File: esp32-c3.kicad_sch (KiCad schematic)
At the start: 11 parts, among them J7 Lichtenprog_conn, Q1 MMBT2222A, Q2 MMBT2222A, U3 ESP32-C3-WROOM-02

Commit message: save before charger replace
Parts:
- renumbered C5 to C15, C6 to C16, J7 to J4, Q1 to Q2, Q2 to Q3, R21 to R15, R25 to R16, R26 to R17, U3 to U7
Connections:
- net +3.3V is gone; now on net 3V3: R15.2

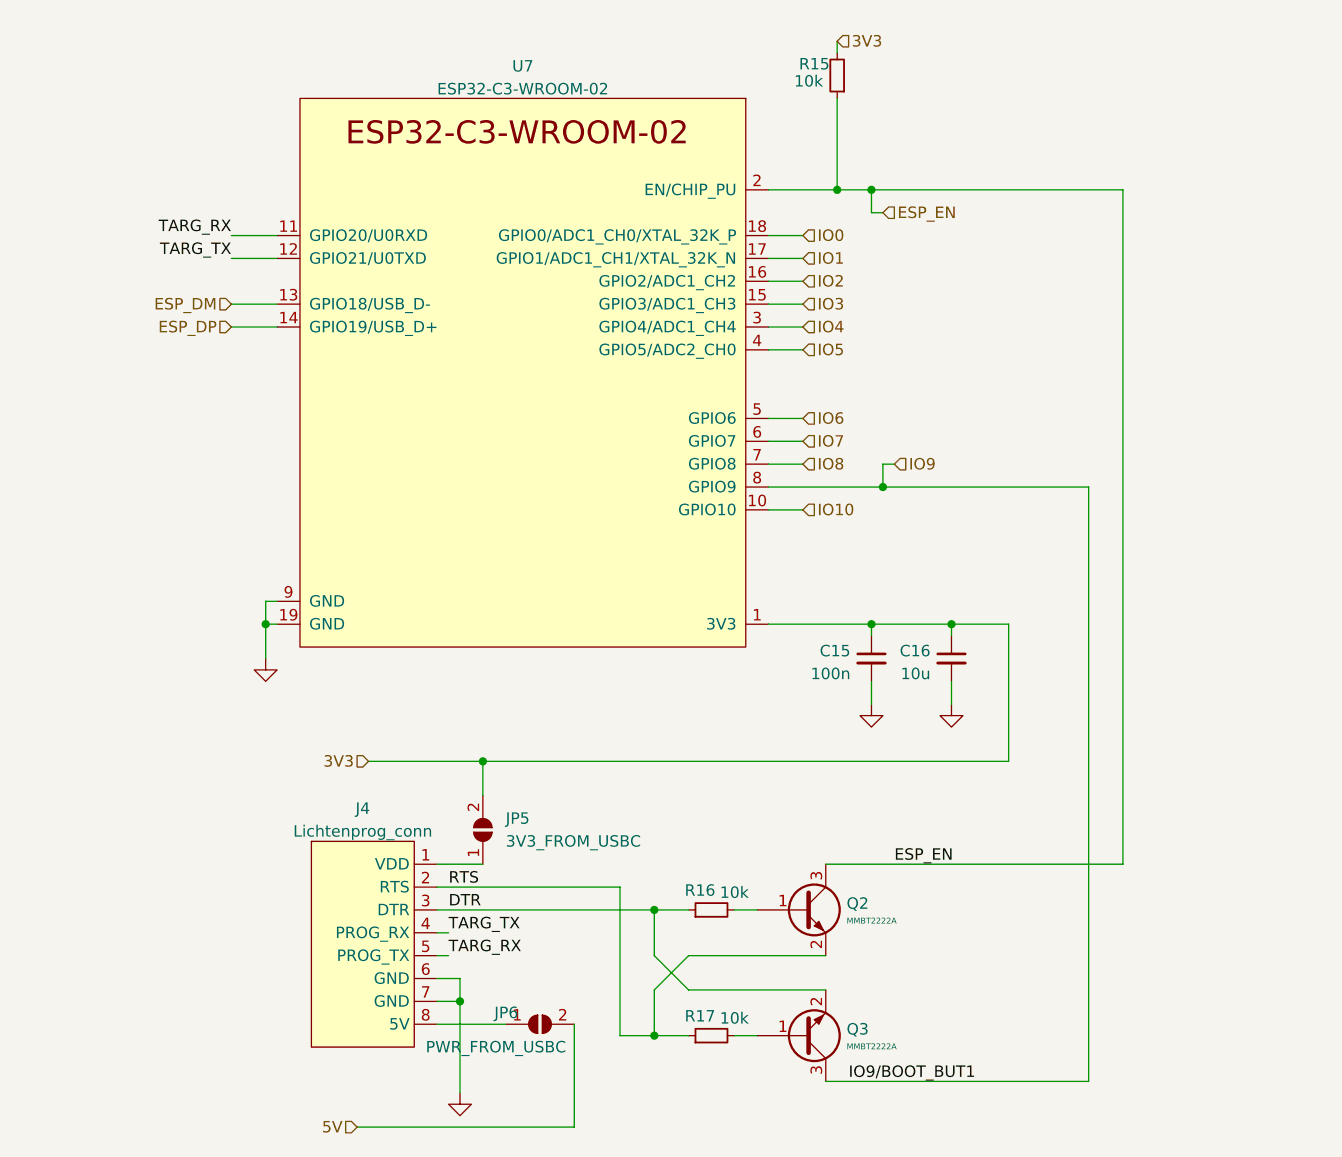
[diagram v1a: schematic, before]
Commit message: connector placement
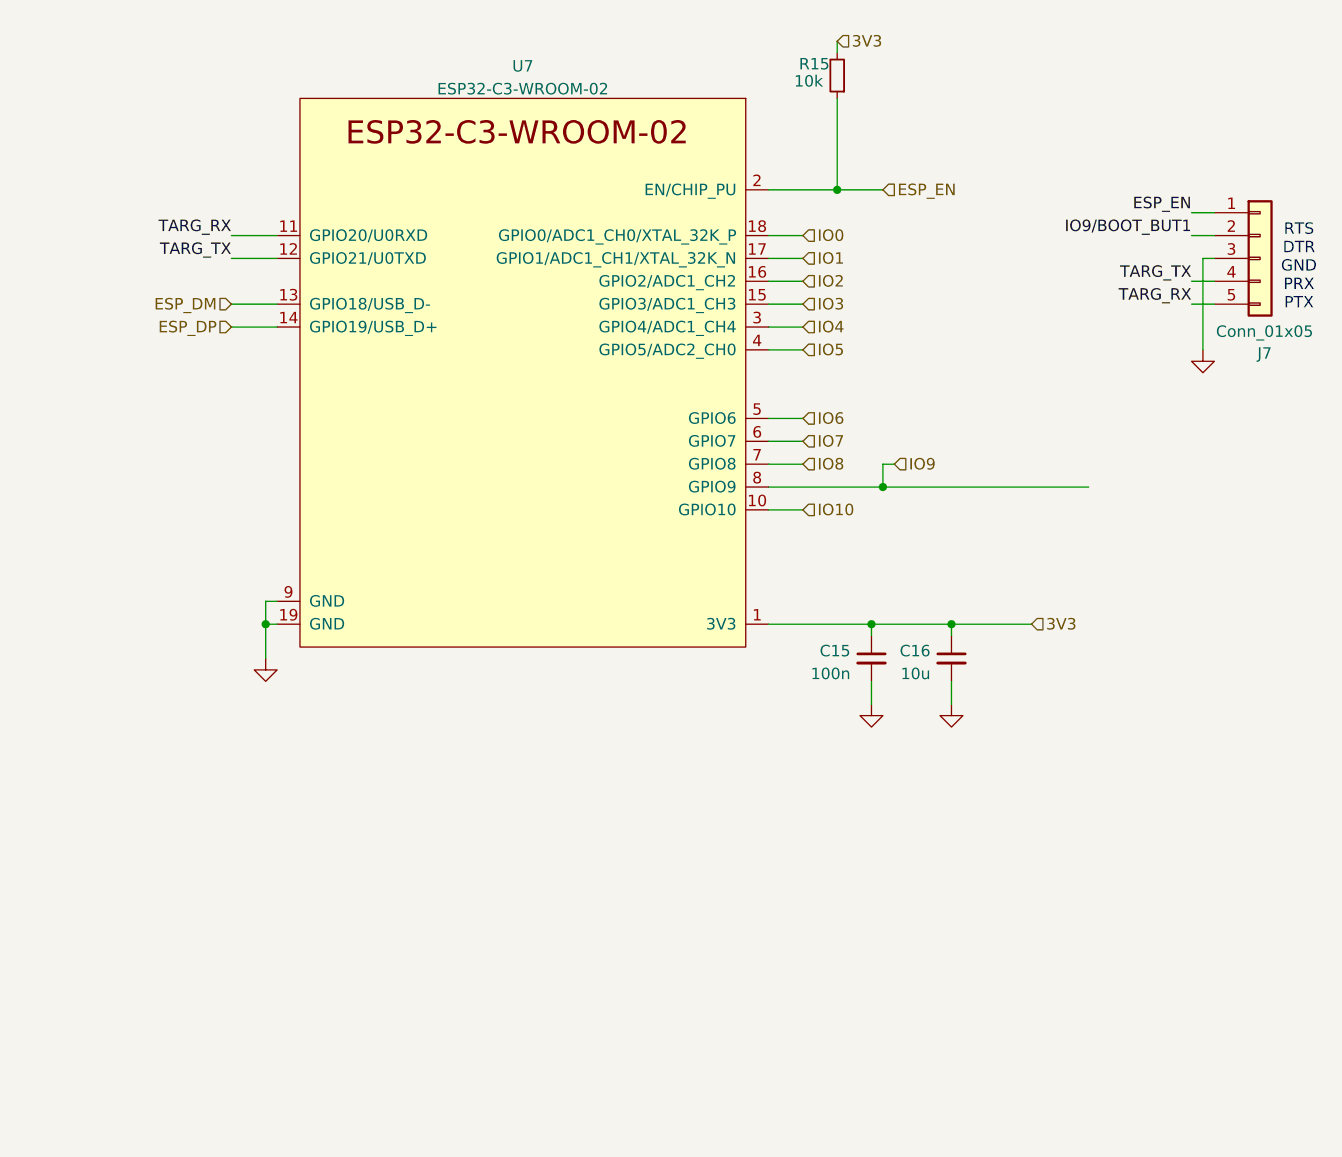
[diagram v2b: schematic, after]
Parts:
- removed J4: Lichtenprog_conn, Critbit_lib:Lichtenprog, symbol Critbit_lib:Lichtenprog_conn
- removed JP5: 3V3_FROM_USBC, Jumper:SolderJumper-2_P1.3mm_Open_TrianglePad1.0x1.5mm, symbol Jumper:SolderJumper_2_Open
- removed JP6: PWR_FROM_USBC, Jumper:SolderJumper-2_P1.3mm_Open_TrianglePad1.0x1.5mm, symbol Jumper:SolderJumper_2_Open
- removed Q2, Q3: MMBT2222A, Package_TO_SOT_SMD:SOT-23, symbol Device:Q_NPN_BEC
- removed R16, R17: 10k, Resistor_SMD:R_0402_1005Metric, symbol Device:R_Small
- added J7: Conn_01x05, Connector_PinHeader_1.27mm:PinHeader_1x05_P1.27mm_Vertical, symbol Connector_Generic:Conn_01x05
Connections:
- net ESP_EN: now also J7.1 (Pin_1)
- net GND: now also J7.3 (Pin_3)
- net TARG_RX: now also J7.5 (Pin_5)
- net TARG_TX: now also J7.4 (Pin_4)
- new net IO9/BOOT_BUT1: J7.2 (Pin_2)
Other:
- note added: "RTS DTR GND PRX PTX"

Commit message: adadadadadadadadadada
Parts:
- C15: LCSC C307331 -> (none)
- C16: LCSC C15525 -> (none)
- R15: LCSC C25744 -> (none)
- U7: LCSC DNP -> (none)
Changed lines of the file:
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@@
-			)
-		)
-		(property "LCSC" "DNP"
-			(at 68.58 96.52 0)
-			(effects
-				(font
-					(size 1.27 1.27)
-				)
-				(hide yes)
 			)
 		)
@@
 			)
 		)
-		(property "LCSC" "C15525"
-			(at 115.57 127 0)
-			(effects
-				(font
-					(size 1.27 1.27)
-				)
-				(hide yes)
-			)
-		)
 		(pin "1"
 		)
@@
 			)
 		)
-		(property "LCSC" "C25744"
-			(at 102.87 62.23 0)
-			(effects
-				(font
-					(size 1.27 1.27)
-				)
-				(hide yes)
-			)
-		)
 		(pin "1"
 		)
@@
 			(at 106.68 127 0)
 			(effects
-				(font
-					(size 1.27 1.27)
-				)
-				(hide yes)
-			)
-		)
-		(property "LCSC" "C307331"
-			(at 106.68 127 0)
-			(effects

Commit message: do backup kids
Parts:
- C16: footprint Capacitor_SMD:C_0402_1005Metric -> Capacitor_SMD:C_0603_1608Metric
- J7: footprint Connector_PinHeader_1.27mm:PinHeader_1x05_P1.27mm_Vertical -> Critbit_lib:sideclutch
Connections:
- net IO9/BOOT_BUT1 is gone; now on net IO9: J7.2 (Pin_2)
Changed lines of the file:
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@@
+	)
+	(junction
+		(at 105.41 74.93)
+		(diameter 0)
+		(color 0 0 0 0)
 	)
 	(junction
@@
 	(wire
 		(pts
+			(xy 130.81 107.95) (xy 130.81 80.01)
+		)
+		(stroke
+			(width 0)
+			(type default)
+		)
+	)
+	(wire
+		(pts
 			(xy 99.06 85.09) (xy 95.25 85.09)
 		)
@@
 	(wire
 		(pts
+			(xy 105.41 74.93) (xy 107.95 74.93)
+		)
+		(stroke
+			(width 0)
+			(type default)
+		)
+	)
+	(wire
+		(pts
 			(xy 109.22 105.41) (xy 107.95 105.41)
 		)
@@
 	(wire
 		(pts
+			(xy 130.81 80.01) (xy 144.78 80.01)
+		)
+		(stroke
+			(width 0)
+			(type default)
+		)
+	)
+	(wire
+		(pts
 			(xy 99.06 100.33) (xy 95.25 100.33)
 		)
@@
 	(wire
 		(pts
+			(xy 105.41 77.47) (xy 105.41 74.93)
+		)
+		(stroke
+			(width 0)
+			(type default)
+		)
+	)
+	(wire
+		(pts
 			(xy 99.06 87.63) (xy 95.25 87.63)
 		)
@@
 	(wire
 		(pts
-			(xy 142.24 80.01) (xy 144.78 80.01)
-		)
-		(stroke
-			(width 0)
-			(type default)
-		)
-	)
-	(wire
-		(pts
 			(xy 106.68 129.54) (xy 106.68 132.08)
 		)
@@
 	(wire
 		(pts
+			(xy 105.41 77.47) (xy 144.78 77.47)
+		)
+		(stroke
+			(width 0)
+			(type default)
+		)
+	)
+	(wire
+		(pts
 			(xy 107.95 105.41) (xy 107.95 107.95)
 		)
@@
 	(wire
 		(pts
-			(xy 142.24 77.47) (xy 144.78 77.47)
-		)
-		(stroke
-			(width 0)
-			(type default)
-		)
-	)
-	(wire
-		(pts
 			(xy 107.95 107.95) (xy 130.81 107.95)
 		)
@@
 	(wire
 		(pts
-			(xy 102.87 74.93) (xy 107.95 74.93)
+			(xy 102.87 74.93) (xy 105.41 74.93)
 		)
 		(stroke
@@
 				(size 1.27 1.27)
 			)
-		)
-	)
-	(label "IO9{slash}BOOT_BUT1"
-		(at 142.24 80.01 180)
-		(fields_autoplaced yes)
-		(effects
-			(font
-				(size 1.27 1.27)
-			)
-			(justify right bottom)
 		)
 	)
@@
 			)
 		)
-		(property "Footprint" "Capacitor_SMD:C_0402_1005Metric"
+		(property "Footprint" "Capacitor_SMD:C_0603_1608Metric"
 			(at 115.57 127 0)
 			(effects
@@
 			)
 		)
-		(property "Footprint" "Connector_PinHeader_1.27mm:PinHeader_1x05_P1.27mm_Vertical"
+		(property "Footprint" "Critbit_lib:sideclutch"
 			(at 149.86 82.55 0)
 			(effects

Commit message: backup 2
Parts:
- J7: footprint Critbit_lib:sideclutch -> Connector_PinHeader_1.27mm:PinHeader_1x05_P1.27mm_Vertical
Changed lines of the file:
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@@
 			)
 		)
-		(property "Footprint" "Critbit_lib:sideclutch"
+		(property "Footprint" "Connector_PinHeader_1.27mm:PinHeader_1x05_P1.27mm_Vertical"
 			(at 149.86 82.55 0)
 			(effects

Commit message: work
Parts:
- removed C15: 100n, Capacitor_SMD:C_0402_1005Metric, symbol Device:C_Small
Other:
- moved on the sheet: C16
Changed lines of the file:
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@@
+	)
+	(junction
+		(at 96.52 123.19)
+		(diameter 0)
+		(color 0 0 0 0)
 	)
 	(junction
@@
 	)
 	(junction
-		(at 106.68 123.19)
-		(diameter 0)
-		(color 0 0 0 0)
-	)
-	(junction
 		(at 102.87 74.93)
 		(diameter 0)
@@
 		(color 0 0 0 0)
 	)
-	(junction
-		(at 115.57 123.19)
-		(diameter 0)
-		(color 0 0 0 0)
-	)
 	(wire
 		(pts
@@
 	(wire
 		(pts
-			(xy 106.68 123.19) (xy 106.68 124.46)
-		)
-		(stroke
-			(width 0)
-			(type default)
-		)
-	)
-	(wire
-		(pts
 			(xy 35.56 80.01) (xy 40.64 80.01)
 		)
@@
 	(wire
 		(pts
-			(xy 106.68 123.19) (xy 115.57 123.19)
-		)
-		(stroke
-			(width 0)
-			(type default)
-		)
-	)
-	(wire
-		(pts
-			(xy 115.57 129.54) (xy 115.57 132.08)
+			(xy 96.52 130.81) (xy 96.52 133.35)
 		)
 		(stroke
@@
 	(wire
 		(pts
-			(xy 115.57 123.19) (xy 124.46 123.19)
-		)
-		(stroke
-			(width 0)
-			(type default)
-		)
-	)
-	(wire
-		(pts
 			(xy 99.06 82.55) (xy 95.25 82.55)
 		)
@@
 	(wire
 		(pts
-			(xy 95.25 123.19) (xy 106.68 123.19)
-		)
-		(stroke
-			(width 0)
-			(type default)
-		)
-	)
-	(wire
-		(pts
-			(xy 115.57 123.19) (xy 115.57 124.46)
+			(xy 95.25 123.19) (xy 96.52 123.19)
+		)
+		(stroke
+			(width 0)
+			(type default)
+		)
+	)
+	(wire
+		(pts
+			(xy 96.52 123.19) (xy 96.52 125.73)
 		)
 		(stroke
@@
 	(wire
 		(pts
+			(xy 96.52 123.19) (xy 100.33 123.19)
+		)
+		(stroke
+			(width 0)
+			(type default)
+		)
+	)
+	(wire
+		(pts
 			(xy 35.56 87.63) (xy 40.64 87.63)
-		)
-		(stroke
-			(width 0)
-			(type default)
-		)
-	)
-	(wire
-		(pts
-			(xy 106.68 129.54) (xy 106.68 132.08)
 		)
 		(stroke
@@
 	(hierarchical_label "3V3"
 		(shape input)
-		(at 124.46 123.19 0)
+		(at 100.33 123.19 0)
 		(fields_autoplaced yes)
 		(effects
@@
 				(path "/5b28c372-d717-46a4-b70a-f55fa1c8ec9b/99d56f3d-90e0-46a1-af9a-78298aac1fc1"
 					(reference "#PWR043")
-					(unit 1)
-				)
-			)
-		)
-	)
-	(symbol
-		(lib_id "power:GND")
-		(at 106.68 132.08 0)
-		(mirror y)
-		(unit 1)
-		(exclude_from_sim no)
-		(in_bom yes)
-		(on_board yes)
-		(dnp no)
-		(fields_autoplaced yes)
-		(property "Reference" "#PWR044"
-			(at 106.68 138.43 0)
-			(effects
-				(font
-					(size 1.27 1.27)
-				)
-				(hide yes)
-			)
-		)
-		(property "Value" "GND"
-			(at 106.68 136.5234 0)
-			(effects
-				(font
-					(size 1.27 1.27)
-				)
-				(hide yes)
-			)
-		)
-		(property "Footprint" ""
-			(at 106.68 132.08 0)
-			(effects
-				(font
-					(size 1.27 1.27)
-				)
-				(hide yes)
-			)
-		)
-		(property "Datasheet" ""
-			(at 106.68 132.08 0)
-			(effects
-				(font
-					(size 1.27 1.27)
-				)
-				(hide yes)
-			)
-		)
-		(property "Description" ""
-			(at 106.68 132.08 0)
-			(effects
-				(font
-					(size 1.27 1.27)
-				)
-				(hide yes)
-			)
-		)
-		(pin "1"
-		)
-		(instances
-			(project "i2current"
-				(path "/5b28c372-d717-46a4-b70a-f55fa1c8ec9b/99d56f3d-90e0-46a1-af9a-78298aac1fc1"
-					(reference "#PWR044")
 					(unit 1)
 				)
@@
 	(symbol
 		(lib_id "Device:C_Small")
-		(at 115.57 127 0)
+		(at 96.52 128.27 0)
 		(mirror y)
 		(unit 1)
@@
 		(fields_autoplaced yes)
 		(property "Reference" "C16"
-			(at 113.2459 126.1716 0)
+			(at 94.1959 127.4416 0)
 			(effects
 				(font
@@
 		)
 		(property "Value" "10u"
-			(at 113.2459 128.7085 0)
+			(at 94.1959 129.9785 0)
 			(effects
 				(font
@@
 		)
 		(property "Footprint" "Capacitor_SMD:C_0603_1608Metric"
-			(at 115.57 127 0)
+			(at 96.52 128.27 0)
 			(effects
 				(font
@@
 		)
 		(property "Datasheet" "~"
-			(at 115.57 127 0)
+			(at 96.52 128.27 0)
 			(effects
 				(font
@@
 		)
 		(property "Description" ""
-			(at 115.57 127 0)
+			(at 96.52 128.27 0)
 			(effects
 				(font
@@
 	(symbol
 		(lib_id "power:GND")
-		(at 115.57 132.08 0)
+		(at 96.52 133.35 0)
 		(mirror y)
 		(unit 1)
@@
 		(fields_autoplaced yes)
 		(property "Reference" "#PWR045"
-			(at 115.57 138.43 0)
+			(at 96.52 139.7 0)
 			(effects
 				(font
@@
 		)
 		(property "Value" "GND"
-			(at 115.57 136.5234 0)
+			(at 96.52 137.7934 0)
 			(effects
 				(font
@@
 		)
 		(property "Footprint" ""
-			(at 115.57 132.08 0)
+			(at 96.52 133.35 0)
 			(effects
 				(font
@@
 		)
 		(property "Datasheet" ""
-			(at 115.57 132.08 0)
+			(at 96.52 133.35 0)
 			(effects
 				(font
@@
 		)
 		(property "Description" ""
-			(at 115.57 132.08 0)
+			(at 96.52 133.35 0)
 			(effects
 				(font
@@
 					(unit 1)
 				)
-			)
-		)
-	)
-	(symbol
-		(lib_id "Device:C_Small")
-		(at 106.68 127 0)
-		(mirror y)
-		(unit 1)
-		(exclude_from_sim no)
-		(in_bom yes)
-		(on_board yes)
-		(dnp no)
-		(fields_autoplaced yes)
-		(property "Reference" "C15"
-			(at 104.3559 126.1716 0)
-			(effects
-				(font
-					(size 1.27 1.27)
-				)
-				(justify left)
-			)
-		)
-		(property "Value" "100n"
-			(at 104.3559 128.7085 0)
-			(effects
-				(font
-					(size 1.27 1.27)
-				)
-				(justify left)
-			)
-		)
-		(property "Footprint" "Capacitor_SMD:C_0402_1005Metric"
-			(at 106.68 127 0)
-			(effects
-				(font
-					(size 1.27 1.27)
-				)
-				(hide yes)
-			)
-		)
-		(property "Datasheet" "~"
-			(at 106.68 127 0)
-			(effects
-				(font
-					(size 1.27 1.27)
-				)
-				(hide yes)
-			)
-		)
-		(property "Description" ""
-			(at 106.68 127 0)
-			(effects
-				(font
-					(size 1.27 1.27)
-				)
-				(hide yes)
-			)
-		)
-		(pin "1"
-		)
-		(pin "2"
-		)
-		(instances
-			(project "i2current"
-				(path "/5b28c372-d717-46a4-b70a-f55fa1c8ec9b/99d56f3d-90e0-46a1-af9a-78298aac1fc1"
-					(reference "C15")
-					(unit 1)
-				)

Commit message: i start order
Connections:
- net TARG_RX renamed ESP_RX
- net TARG_TX renamed ESP_TX
